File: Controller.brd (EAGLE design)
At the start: 100 x 66 mm, 21 parts, among them IC1 TB6612FNG

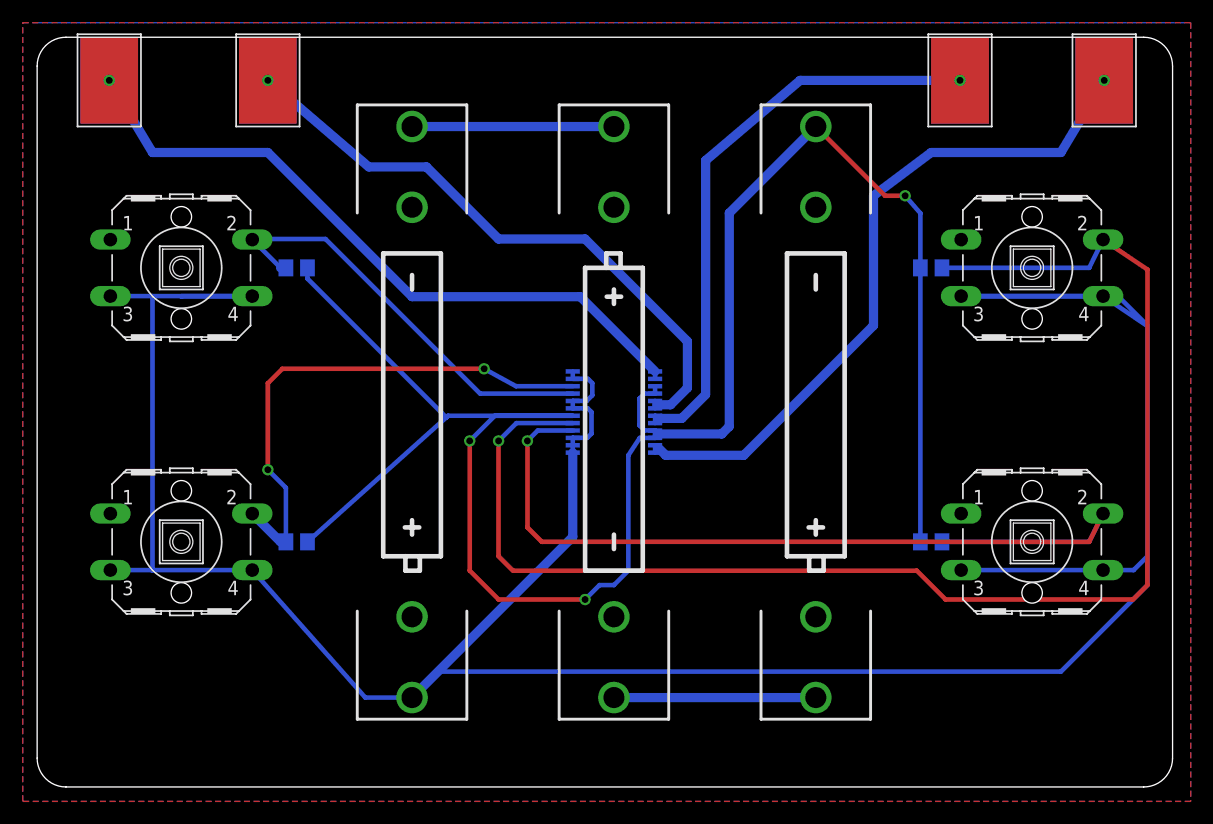
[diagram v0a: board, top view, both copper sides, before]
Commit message: add diode to board and schematic
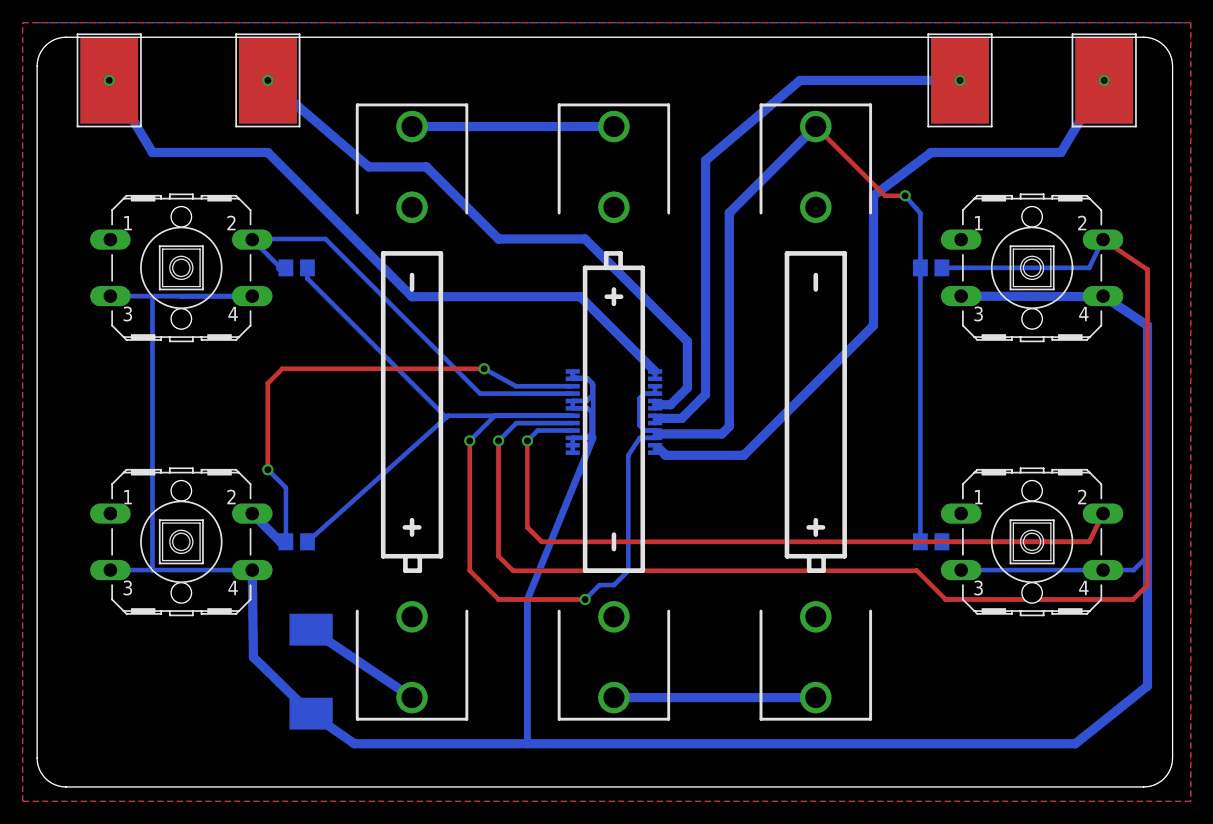
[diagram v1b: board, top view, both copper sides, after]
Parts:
- added D1: (no value), diode:SMC
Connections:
- new net N$3: BAT1.PWR@1, D1.A
- net VCC: now also D1.C; no longer BAT1.PWR@1
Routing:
- net VCC: track 278.6 -> 298.1 mm
- net N$3: track 0.00 -> 10.7 mm
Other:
- board text added: "Robotcrafts v2.1"
- board text removed: "Robotcrafts v2.0"
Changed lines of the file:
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@@
 <wire x1="97.46" y1="66.03" x2="2.54" y2="66.03" width="0" layer="20"/>
 <wire x1="2.54" y1="66.03" x2="0" y2="63.49" width="0" layer="20" curve="90"/>
-<text x="97.79" y="6.35" size="1.9304" layer="26" rot="MR0">Robotcrafts v2.0</text>
+<text x="97.79" y="6.35" size="1.9304" layer="26" rot="MR0">Robotcrafts v2.1</text>
 <text x="97.79" y="2.54" size="1.27" layer="26" rot="MR0">by Joshua Gruenstein
 Camp Good Grief</text>
@@
 </element>
 <element name="GOLD_ORB_SM1" library="bfl" package="OSHW1" value="OSHWLOGO_GOLD_ORB_MED" x="15.24" y="1.27" smashed="yes" rot="MR0"/>
+<element name="D1" library="diode" package="SMC" value="" x="24.13" y="10.16" rot="MR90"/>
 </elements>
 <signals>
@@
 </signal>
 <signal name="VCC">
-<contactref element="BAT1" pad="PWR@1"/>
 <contactref element="L_FWD_BTN" pad="3"/>
 <contactref element="L_FWD_BTN" pad="4"/>
@@
 <wire x1="47.175" y1="30.745" x2="47.175" y2="30.095" width="0.4064" layer="16"/>
 <wire x1="47.175" y1="30.095" x2="47.175" y2="29.445" width="0.4064" layer="16"/>
-<wire x1="33.02" y1="7.874" x2="47.175" y2="22.029" width="0.8128" layer="16"/>
-<wire x1="47.175" y1="22.029" x2="47.175" y2="29.445" width="0.8128" layer="16"/>
 <wire x1="18.9484" y1="43.2308" x2="10.16" y2="43.2308" width="0.4064" layer="16"/>
 <wire x1="10.16" y1="43.2308" x2="6.4516" y2="43.2308" width="0.4064" layer="16"/>
-<wire x1="33.02" y1="7.874" x2="28.9052" y2="7.874" width="0.4064" layer="16"/>
-<wire x1="28.9052" y1="7.874" x2="18.9484" y2="19.1008" width="0.4064" layer="16"/>
 <wire x1="18.9484" y1="19.1008" x2="10.2108" y2="19.1008" width="0.4064" layer="16"/>
 <wire x1="10.2108" y1="19.1008" x2="6.4516" y2="19.1008" width="0.4064" layer="16"/>
@@
 <wire x1="97.79" y1="20.32" x2="97.79" y2="40.5892" width="0.4064" layer="16"/>
 <wire x1="97.79" y1="40.5892" x2="93.8784" y2="43.2308" width="0.4064" layer="16"/>
-<wire x1="81.3816" y1="43.2308" x2="95.1992" y2="43.2308" width="0.4064" layer="16"/>
-<wire x1="95.1992" y1="43.2308" x2="97.79" y2="40.64" width="0.4064" layer="16"/>
-<wire x1="97.79" y1="40.64" x2="97.79" y2="17.78" width="0.4064" layer="16"/>
-<wire x1="97.79" y1="17.78" x2="90.17" y2="10.16" width="0.4064" layer="16"/>
-<wire x1="90.17" y1="10.16" x2="35.306" y2="10.16" width="0.4064" layer="16"/>
-<wire x1="35.306" y1="10.16" x2="33.02" y2="7.874" width="0.4064" layer="16"/>
+<contactref element="D1" pad="C"/>
+<wire x1="24.13" y1="6.46" x2="19.05" y2="11.43" width="0.8128" layer="16"/>
+<wire x1="19.05" y1="11.43" x2="18.9484" y2="19.1008" width="0.8128" layer="16"/>
+<wire x1="81.3816" y1="43.2308" x2="93.98" y2="43.18" width="0.8128" layer="16"/>
+<wire x1="93.98" y1="43.18" x2="97.79" y2="40.64" width="0.8128" layer="16"/>
+<wire x1="97.79" y1="40.64" x2="97.79" y2="8.89" width="0.8128" layer="16"/>
+<wire x1="97.79" y1="8.89" x2="91.44" y2="3.81" width="0.8128" layer="16"/>
+<wire x1="91.44" y1="3.81" x2="43.18" y2="3.81" width="0.8128" layer="16"/>
+<wire x1="43.18" y1="3.81" x2="27.94" y2="3.81" width="0.8128" layer="16"/>
+<wire x1="27.94" y1="3.81" x2="24.13" y2="6.46" width="0.8128" layer="16"/>
+<wire x1="47.175" y1="36.595" x2="47.191834375" y2="36.08425625" width="0.4064" layer="16"/>
+<wire x1="47.191834375" y1="36.08425625" x2="48.485921875" y2="35.9767" width="0.4064" layer="16"/>
+<wire x1="48.485921875" y1="35.9767" x2="48.96970625" y2="35.38515625" width="0.4064" layer="16"/>
+<wire x1="48.96970625" y1="35.38515625" x2="48.96970625" y2="30.760346875" width="0.4064" layer="16"/>
+<wire x1="48.96970625" y1="30.760346875" x2="43.18" y2="16.51" width="0.6096" layer="16"/>
+<wire x1="43.18" y1="16.51" x2="43.18" y2="3.81" width="0.6096" layer="16"/>
 </signal>
 <signal name="GND">
@@
 <wire x1="90.17" y1="55.88" x2="93.98" y2="62.23" width="0.8128" layer="16"/>
 </signal>
+<signal name="N$3">
+<contactref element="D1" pad="A"/>
+<contactref element="BAT1" pad="PWR@1"/>
+<wire x1="33.02" y1="7.874" x2="24.13" y2="13.86" width="0.8128" layer="16"/>
+</signal>
 </signals>
